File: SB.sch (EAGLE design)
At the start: 30 parts, among them IC1 ATMEGA32U4NT-TQFP, J1 USB-6P-SMT, J3 AUDIO-JACK-PJ321, J4 NO/NC, J5 RJ10-WURTH, K1 HE721C-DIP, Q1 2N7002

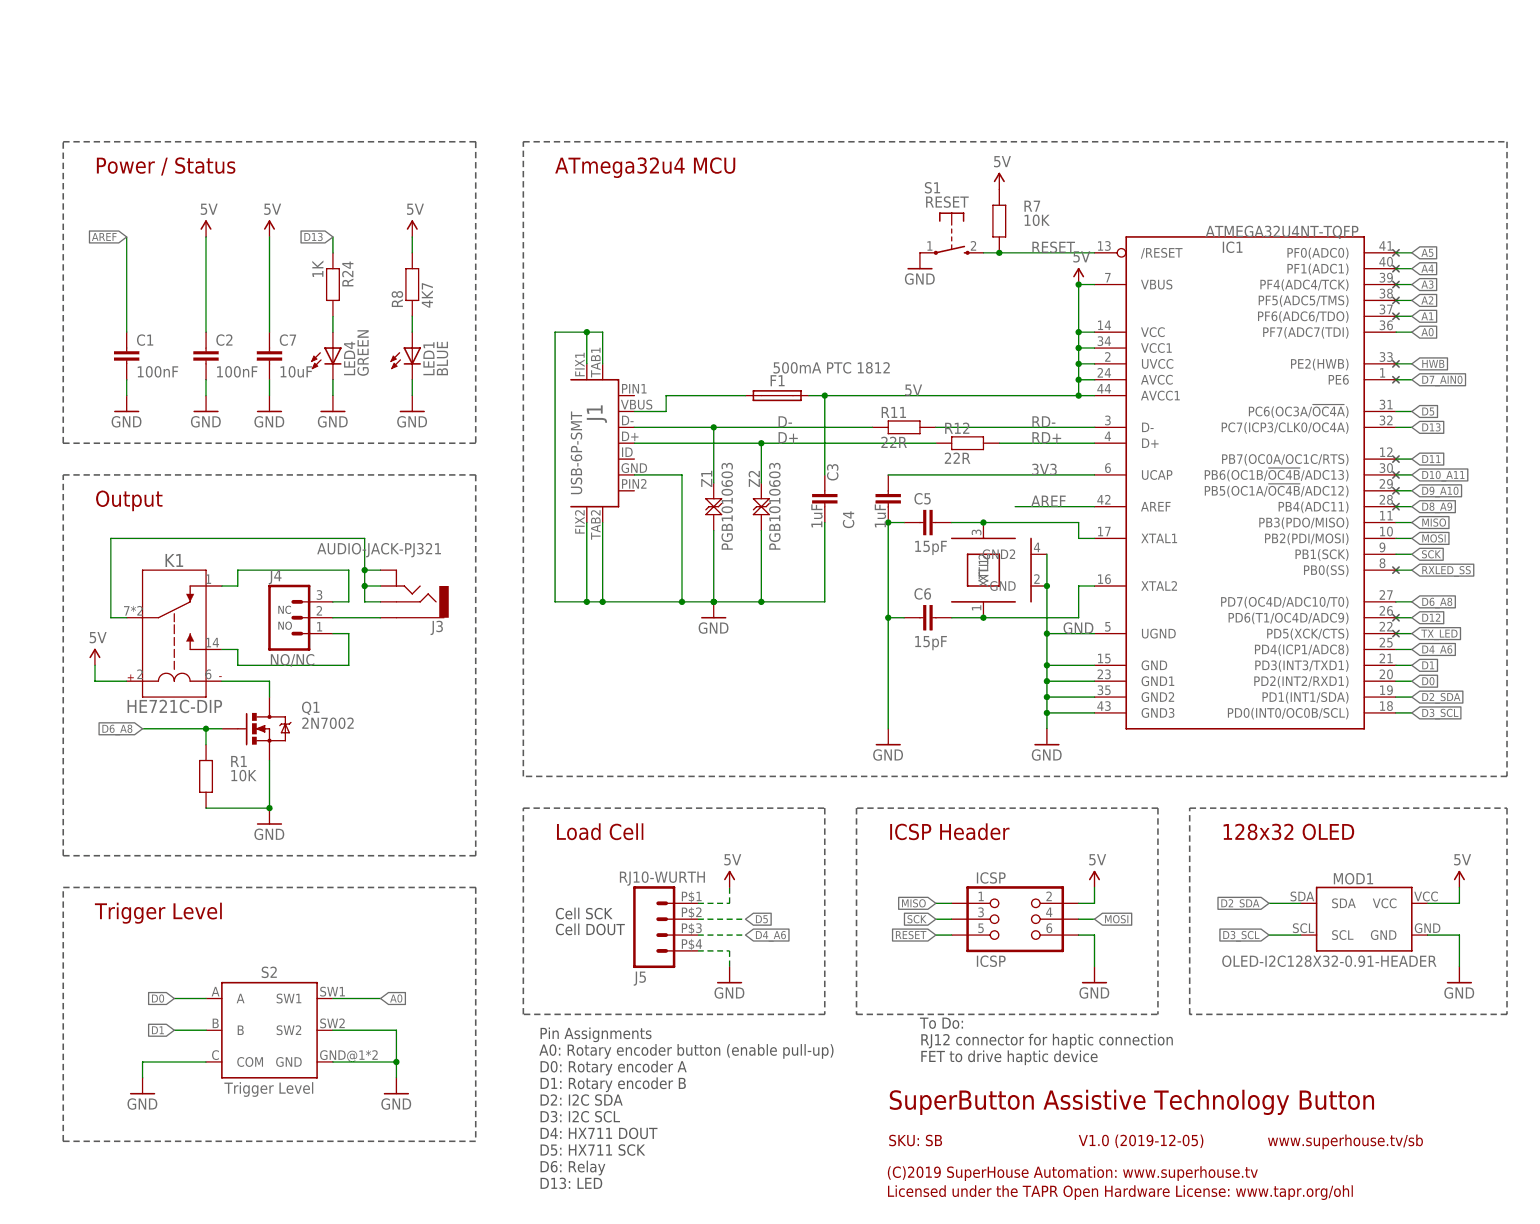
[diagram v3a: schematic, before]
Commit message: Replaced RJ10 socket with RJ12 and added haptic feedback output
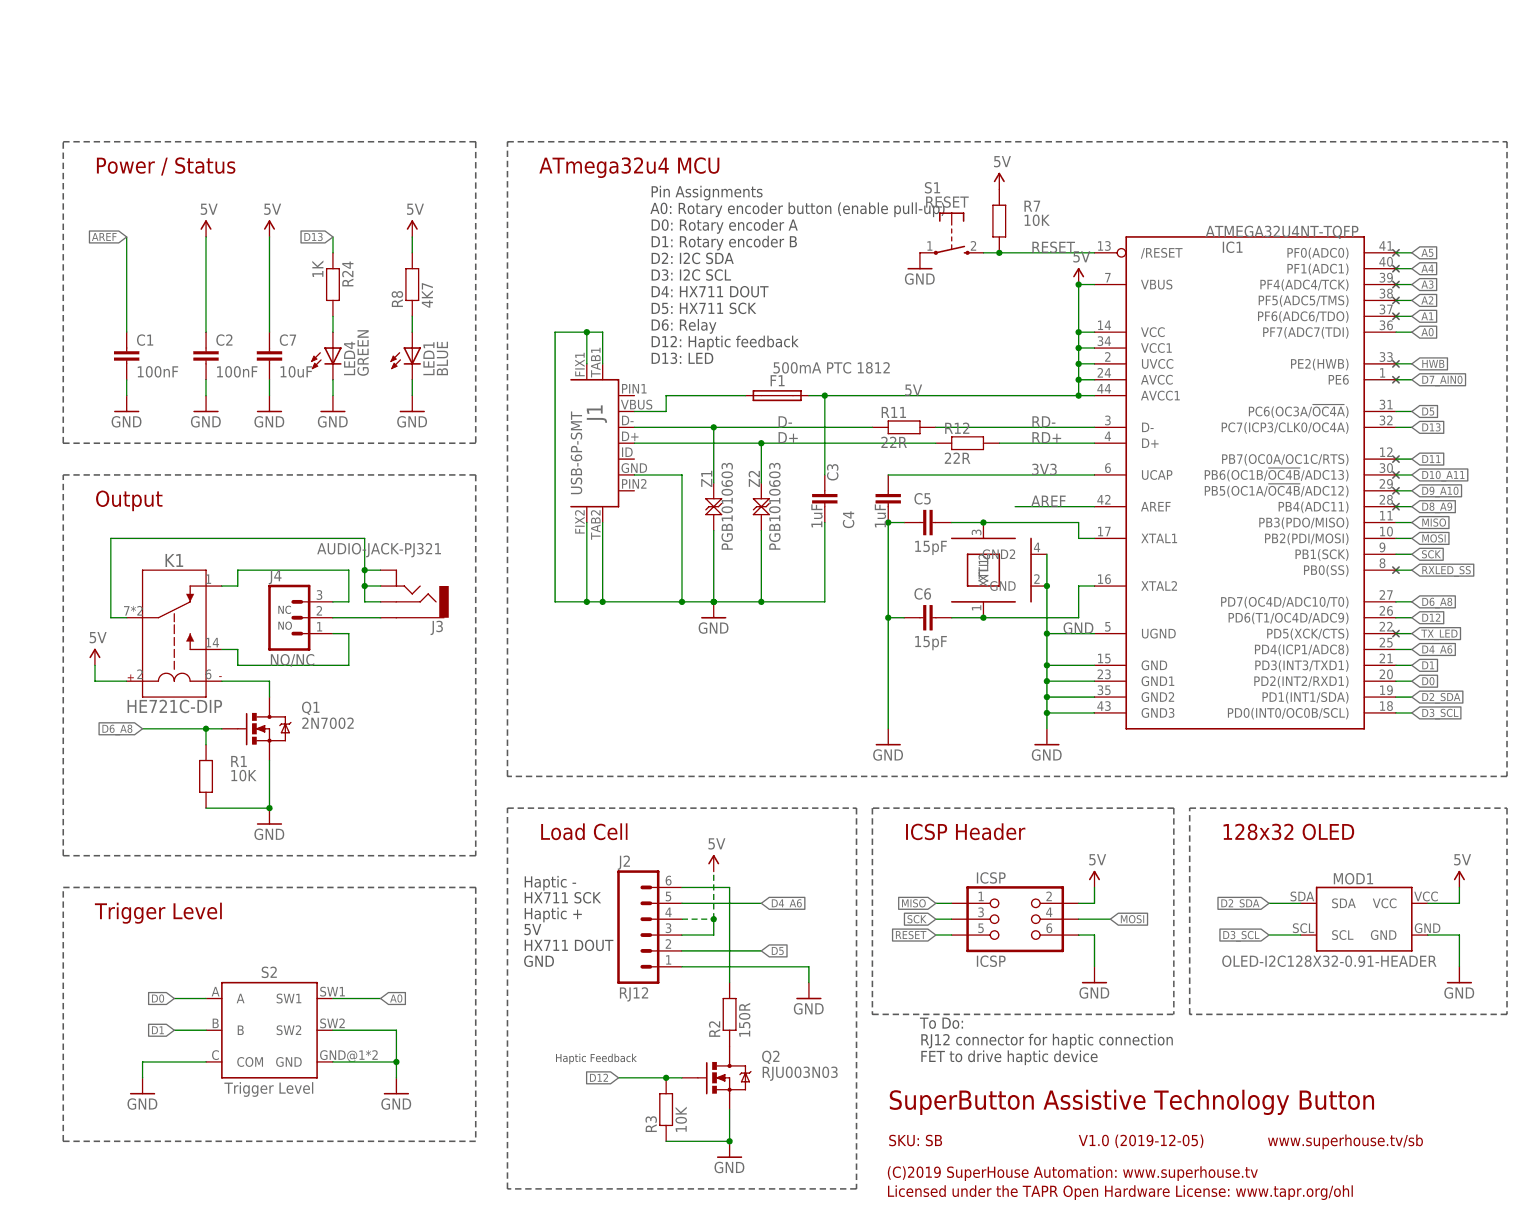
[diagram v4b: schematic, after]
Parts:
- removed J5: RJ10-WURTH, SuperHouse-Connectors:RJ10-WURTH
- added J2: RJ12, SuperHouse-Connectors:RJ12
- added Q2: RJU003N03, SuperHouse-DiscreteSemi:MOSFET-NCHANNEL-323
- added R2: 150R, SuperHouse-DiscreteSemi:RESISTOR0603
- added R3: 10K, SuperHouse-DiscreteSemi:RESISTOR0603
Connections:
- new net N$2: J2.6, R2.2
- new net N$8: Q2.D, R2.1
- net 5V: now also J2.3, J2.4; no longer J5.1
- net D12: now also Q2.G, R3.2
- net D4_A6: now also J2.5; no longer J5.3
- net D5: now also J2.2; no longer J5.2
- net GND: now also J2.1, Q2.S, R3.1; no longer J5.4
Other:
- note added: "5V"
- note added: "GND"
- note added: "HX711 DOUT"
- note added: "HX711 SCK"
- note added: "Haptic +"
- note added: "Haptic -"
- note added: "Haptic Feedback"
- note added: "Pin Assignments A0: Rotary encoder button (enable pull-up) D0: Rotary encoder A D1: Rotary encoder B D2: I2C SDA D3: I2C SCL D4: HX711 DOUT D5: HX711 SCK D6: Relay D12: Haptic feedback D13: LED"
- note removed: "Cell DOUT"
- note removed: "Cell SCK"
- note removed: "Pin Assignments A0: Rotary encoder button (enable pull-up) D0: Rotary encoder A D1: Rotary encoder B D2: I2C SDA D3: I2C SCL D4: HX711 DOUT D5: HX711 SCK D6: Relay D13: LED"

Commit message: Tweaks and cleanup, hopefully for v1.1 release
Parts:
- added R4: 10K, SuperHouse-DiscreteSemi:RESISTOR0603
- Q2: value RJU003N03 -> 2N7002; device SuperHouse-DiscreteSemi:MOSFET-NCHANNEL-323 -> SuperHouse-DiscreteSemi:MOSFET-NCHANNEL-233
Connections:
- net 5V: now also R4.2
- net A0: now also R4.1
- net N$7: no longer J3.2
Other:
- note added: "To Do: Pullup on A0 Split stereo socket"
- note added: "V1.1 (2019-12-19)"
- note removed: "To Do: RJ12 connector for haptic connection FET to drive haptic device"
- note removed: "V1.0 (2019-12-05)"
- moved on the sheet: S2

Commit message: Added HX711 strain gauge amplifier directly on controller instead of external
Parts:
- removed J1: USB-6P-SMT, SuperHouse-Connectors:USB-6P-SMT
- added C10, C12: 10uF, SuperHouse-DiscreteSemi:CAP0603
- added C11, C8, C9: 100nF, SuperHouse-DiscreteSemi:CAP0603
- added IC2: HX711-SOP16L, SuperHouse-ICs:HX711-SOP16L
- added J5: USB-C-16P-16P, SuperHouse-Connectors:USB-C-16P-16P
- added L1: 3.3uH, SuperHouse-DiscreteSemi:INDUCTOR0603
- added Q3: 2N3906, SuperHouse-DiscreteSemi:TRANS_PNPMMBT3906LT1SOT23-BEC
- added R10, R9: 100R, SuperHouse-DiscreteSemi:RESISTOR0603
- added R13: 10K, SuperHouse-DiscreteSemi:RESISTOR0603
- added R14: 8K2, SuperHouse-DiscreteSemi:RESISTOR0603
- added R5, R6: 4K7, SuperHouse-DiscreteSemi:RESISTOR0603
- MOD1: value OLED-I2C128X32-0.91-HEADER -> OLED-I2C-128X32-0.91; device SuperHouse-Displays:OLED-I2C128X32-0.91-HEADER -> SuperHouse-Displays:OLED-I2C-128X32-0.91
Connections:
- new net A+: J2.4, R10.1
- new net A-: J2.3, R9.1
- new net E+: C10.1, C11.1, J2.1, L1.1
- new net N$10: J5.CC2, R6.2
- new net N$13: J5.CC1, R5.2
- new net N$14: C9.1, IC2.INA-, R9.2
- new net N$15: C9.2, IC2.INA+, R10.2
- new net N$16: IC2.AVDD, L1.2, Q3.C, R13.2
- new net N$17: C8.1, IC2.VBG
- new net N$20: IC2.BASE, Q3.B
- new net N$21: IC2.VFB, R13.1, R14.2
- net 5V: now also C12.1, IC2.DVDD, IC2.VSUP, J2.6, Q3.E; no longer J2.3, J2.4
- net D+: now also J5.D+; no longer J1.D+
- net D-: now also J5.D-; no longer J1.D-
- net D4_A6: now also IC2.PD_SCK; no longer J2.5
- net D5: now also IC2.DOUT; no longer J2.2
- net GND: now also C10.2, C11.2, C12.2, C8.2, IC2.AGND, IC2.RATE, IC2.XI, J2.2, J5.GND, R14.1, R5.1, R6.1; no longer J1.FIX1, J1.FIX2, J1.GND, J1.TAB1, J1.TAB2, J2.1
- net N$2: now also J2.5; no longer J2.6
- net USB+: now also J5.VBUS; no longer J1.VBUS
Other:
- note added: "(C)2020 SuperHouse Automation: www.superhouse.tv"
- note added: "A+"
- note added: "A-"
- note added: "E+"
- note added: "E-"
- note added: "Haptic Feedback Control"
- note added: "Load Cell Amplifier"
- note added: "Sample rate set to 10Hz by pulling RATE pin low"
- note added: "V2.0 (2020-01-11)"
- note removed: "(C)2019 SuperHouse Automation: www.superhouse.tv"
- note removed: "5V"
- note removed: "GND"
- note removed: "HX711 DOUT"
- note removed: "HX711 SCK"
- note removed: "Haptic Feedback"
- note removed: "Load Cell"
- note removed: "V1.1 (2019-12-19)"

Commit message: Routing for v2.0 release
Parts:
- removed J4: NO/NC, SuperHouse-Connectors:M03-PIN
- added SW1: SWITCH-SPDT-4TABSSMT, SuperHouse-Switches:SWITCH-SPDT-4TABSSMT
- MOD1: value OLED-I2C-128X32-0.91 -> OLED-I2C-128X32-0.91-HEADER; device SuperHouse-Displays:OLED-I2C-128X32-0.91 -> SuperHouse-Displays:OLED-I2C-128X32-0.91-HEADER
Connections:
- net A+: now also J2.3; no longer J2.4
- net A-: now also J2.4; no longer J2.3
- net GND: now also SW1.MNT@1, SW1.MNT@2, SW1.MNT@3, SW1.MNT@4
- net N$4: now also K1.NO, SW1.B; no longer J4.3, K1.NC
- net N$6: now also K1.NC, SW1.A; no longer J4.1, K1.NO
- net N$9: now also SW1.COM; no longer J4.2
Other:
- note added: "V2.0 (2020-01-13)"
- note removed: "V2.0 (2020-01-11)"
- moved on the sheet: C9, R10, R9
